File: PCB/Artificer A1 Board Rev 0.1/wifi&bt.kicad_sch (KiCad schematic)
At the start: 13 parts

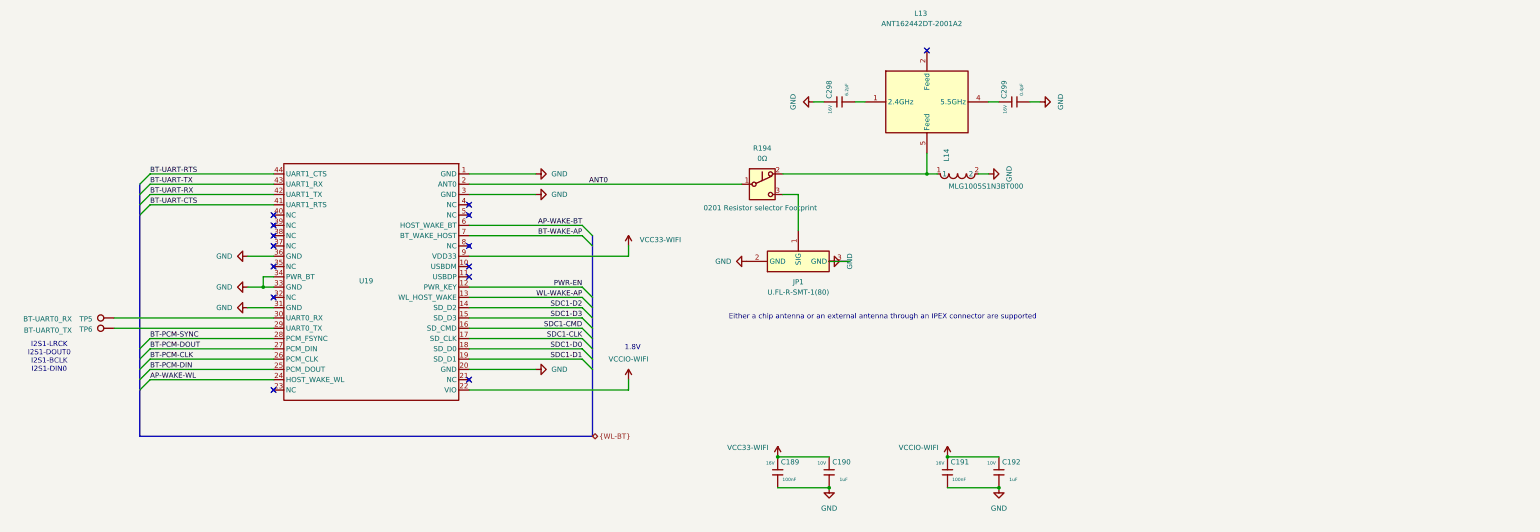
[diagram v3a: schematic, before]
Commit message: optimized copper pour, added LEDs
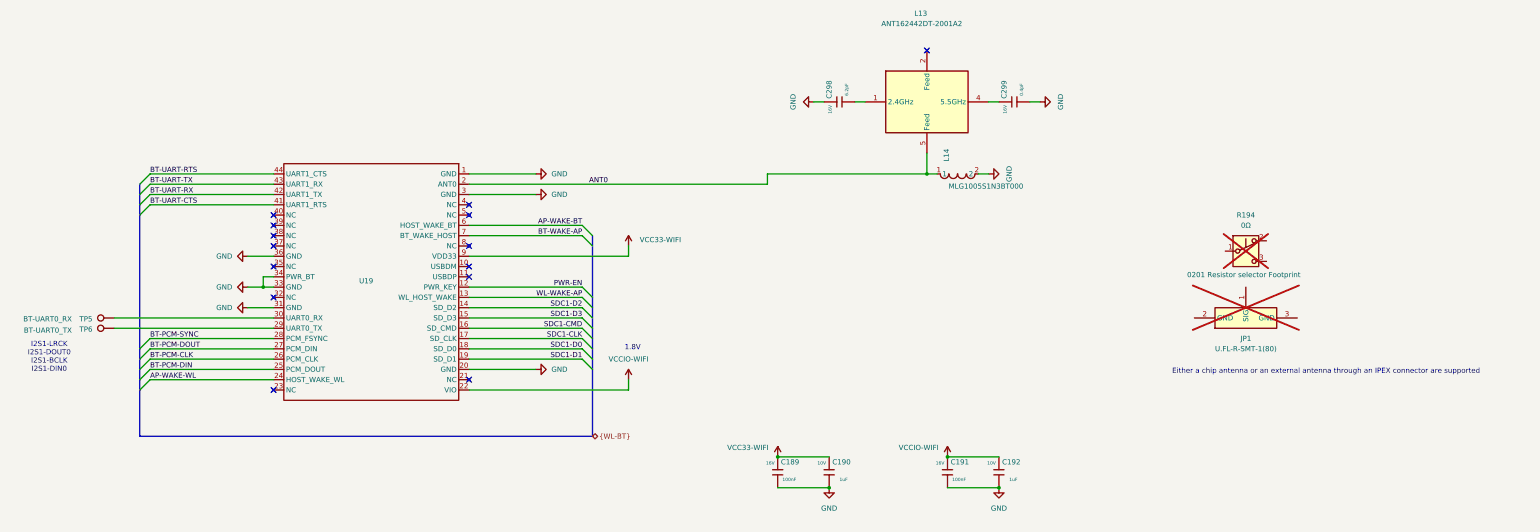
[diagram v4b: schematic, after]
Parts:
- JP1, R194: now not fitted; now left out of the parts list
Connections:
- net ANT0: now also L13.5 (Feed), L14.1; no longer R194.1 (B)
- net GND: no longer JP1.2 (GND), JP1.3 (GND)
- net at R194.3 (C): no longer JP1.1 (SIG)
- now unconnected: R194.2 (A)
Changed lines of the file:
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@@
 	(text "Either a chip antenna or an external antenna through an IPEX connector are supported"
 		(exclude_from_sim no)
-		(at 230.378 107.696 0)
+		(at 339.852 121.158 0)
 		(effects
 			(font
@@
 		)
 	)
-	(bus
+	(wire
 		(pts
-			(xy 158.75 110.49) (xy 158.75 113.03)
+			(xy 201.93 72.39) (xy 201.93 74.93)
 		)
 		(stroke
@@
 		)
 	)
-	(wire
+	(bus
 		(pts
-			(xy 80.01 123.19) (xy 49.53 123.19)
+			(xy 158.75 110.49) (xy 158.75 113.03)
 		)
 		(stroke
@@
 	(wire
 		(pts
-			(xy 205.74 72.39) (xy 241.3 72.39)
+			(xy 80.01 123.19) (xy 49.53 123.19)
 		)
 		(stroke
@@
 		)
 	)
-	(wire
-		(pts
-			(xy 209.55 77.47) (xy 209.55 86.36)
-		)
-		(stroke
-			(width 0)
-			(type default)
-		)
-	)
 	(bus
 		(pts
@@
 	(wire
 		(pts
-			(xy 128.27 74.93) (xy 195.58 74.93)
+			(xy 128.27 74.93) (xy 201.93 74.93)
 		)
 		(stroke
@@
 	(wire
 		(pts
-			(xy 205.74 77.47) (xy 209.55 77.47)
-		)
-		(stroke
-			(width 0)
-			(type default)
-		)
-	)
-	(wire
-		(pts
 			(xy 80.01 100.33) (xy 77.47 100.33)
 		)
@@
 	(wire
 		(pts
-			(xy 215.9 54.61) (xy 213.36 54.61)
+			(xy 201.93 72.39) (xy 241.3 72.39)
 		)
 		(stroke
@@
 	(wire
 		(pts
-			(xy 80.01 72.39) (xy 49.53 72.39)
+			(xy 215.9 54.61) (xy 213.36 54.61)
 		)
 		(stroke
@@
 	(wire
 		(pts
-			(xy 156.21 105.41) (xy 128.27 105.41)
+			(xy 80.01 72.39) (xy 49.53 72.39)
 		)
 		(stroke
@@
 	(wire
 		(pts
-			(xy 80.01 118.11) (xy 49.53 118.11)
+			(xy 156.21 105.41) (xy 128.27 105.41)
 		)
 		(stroke
@@
 	(wire
 		(pts
-			(xy 222.25 93.98) (xy 217.17 93.98)
+			(xy 80.01 118.11) (xy 49.53 118.11)
 		)
 		(stroke
@@
 	)
 	(symbol
-		(lib_id "power:GND")
-		(at 217.17 93.98 90)
-		(mirror x)
-		(unit 1)
-		(body_style 1)
-		(exclude_from_sim no)
-		(in_bom yes)
-		(on_board yes)
-		(in_pos_files yes)
-		(dnp no)
-		(fields_autoplaced yes)
-		(property "Reference" "#PWR0420"
-			(at 223.52 93.98 0)
-			(hide yes)
-			(show_name no)
-			(do_not_autoplace no)
-			(effects
-				(font
-					(size 1.27 1.27)
-				)
-			)
-		)
-		(property "Value" "GND"
-			(at 222.25 93.98 0)
-			(show_name no)
-			(do_not_autoplace no)
-			(effects
-				(font
-					(size 1.27 1.27)
-				)
-			)
-		)
-		(property "Footprint" ""
-			(at 217.17 93.98 0)
-			(hide yes)
-			(show_name no)
-			(do_not_autoplace no)
-			(effects
-				(font
-					(size 1.27 1.27)
-				)
-			)
-		)
-		(property "Datasheet" ""
-			(at 217.17 93.98 0)
-			(hide yes)
-			(show_name no)
-			(do_not_autoplace no)
-			(effects
-				(font
-					(size 1.27 1.27)
-				)
-			)
-		)
-		(property "Description" "Power symbol creates a global label with name \"GND\" , ground"
-			(at 217.17 93.98 0)
-			(hide yes)
-			(show_name no)
-			(do_not_autoplace no)
-			(effects
-				(font
-					(size 1.27 1.27)
-				)
-			)
-		)
-		(pin "1"
-		)
-		(instances
-			(project "Artificer A1 Board Rev 0.1"
-				(path "/7c37bdb5-94b0-4567-b5ec-a879db855389/bb518e39-315f-4fac-931f-ad14a14e5ca9"
-					(reference "#PWR0420")
-					(unit 1)
-				)
-			)
-		)
-	)
-	(symbol
 		(lib_id "easyeda:ANT162442DT-2001A2")
 		(at 241.3 54.61 0)
@@
 	(symbol
 		(lib_id "Switch:SW_Push_SPDT")
-		(at 200.66 74.93 0)
+		(at 320.04 91.44 0)
 		(unit 1)
 		(body_style 1)
-		(exclude_from_sim no)
-		(in_bom yes)
-		(on_board yes)
-		(in_pos_files yes)
-		(dnp no)
+		(exclude_from_sim yes)
+		(in_bom no)
+		(on_board no)
+		(in_pos_files no)
+		(dnp yes)
 		(property "Reference" "R194"
-			(at 200.66 66.04 0)
+			(at 320.04 82.55 0)
 			(show_name no)
 			(do_not_autoplace no)
@@
 		)
 		(property "Value" "0Ω"
-			(at 200.66 68.58 0)
+			(at 320.04 85.09 0)
 			(show_name no)
 			(do_not_autoplace no)
@@
 		)
 		(property "Footprint" "custom footprints:RF_Select_0201_L_Shape"
-			(at 200.66 74.93 0)
+			(at 320.04 91.44 0)
 			(hide yes)
 			(show_name no)
@@
 		)
 		(property "Datasheet" ""
-			(at 200.66 74.93 0)
+			(at 320.04 91.44 0)
 			(hide yes)
 			(show_name no)
@@
 		)
 		(property "Description" "0201 Resistor selector Footprint"
-			(at 200.152 80.772 0)
+			(at 319.532 97.282 0)
 			(show_name no)
 			(do_not_autoplace no)
@@
 	(symbol
 		(lib_id "easyeda:U.FL-R-SMT-1(80)")
-		(at 209.55 91.44 0)
+		(at 320.04 105.41 0)
 		(mirror x)
 		(unit 1)
 		(body_style 1)
-		(exclude_from_sim no)
-		(in_bom yes)
-		(on_board yes)
-		(in_pos_files yes)
-		(dnp no)
+		(exclude_from_sim yes)
+		(in_bom no)
+		(on_board no)
+		(in_pos_files no)
+		(dnp yes)
 		(fields_autoplaced yes)
 		(property "Reference" "JP1"
-			(at 209.55 99.06 0)
+			(at 320.04 113.03 0)
 			(show_name no)
 			(do_not_autoplace no)
@@
 		)
 		(property "Value" "U.FL-R-SMT-1(80)"
-			(at 209.55 101.6 0)
+			(at 320.04 115.57 0)
 			(show_name no)
 			(do_not_autoplace no)
@@
 		)
 		(property "Footprint" "easyeda:RF-SMD_FRF05002-JSS103M"
-			(at 209.55 78.74 0)
+			(at 320.04 92.71 0)
 			(hide yes)
 			(show_name no)
@@
 		)
 		(property "Datasheet" "https://lcsc.com/product-detail/Connectors_HRS_U-FL-R-SMT-1-80_3310472280-IPE-XBoard-end-IPXConnector-SMD_C88374.html"
-			(at 209.55 76.2 0)
+			(at 320.04 90.17 0)
 			(hide yes)
 			(show_name no)
@@
 		)
 		(property "Description" ""
-			(at 209.55 91.44 0)
+			(at 320.04 105.41 0)
 			(hide yes)
 			(show_name no)
@@
 		)
 		(property "LCSC Part" "C88374"
-			(at 209.55 73.66 0)
+			(at 320.04 87.63 0)
 			(hide yes)
 			(show_name no)
@@
 					(unit 1)
 				)
-			)
-		)
-	)
-	(symbol
-		(lib_id "power:GND")
-		(at 196.85 93.98 270)
-		(mirror x)
-		(unit 1)
-		(body_style 1)
-		(exclude_from_sim no)
-		(in_bom yes)
-		(on_board yes)
-		(in_pos_files yes)
-		(dnp no)
-		(fields_autoplaced yes)
-		(property "Reference" "#PWR0417"
-			(at 190.5 93.98 0)
-			(hide yes)
-			(show_name no)
-			(do_not_autoplace no)
-			(effects
-				(font
-					(size 1.27 1.27)
-				)
-			)
-		)
-		(property "Value" "GND"
-			(at 193.04 93.9799 90)
-			(show_name no)
-			(do_not_autoplace no)
-			(effects
-				(font
-					(size 1.27 1.27)
-				)
-				(justify right)
-			)
-		)
-		(property "Footprint" ""
-			(at 196.85 93.98 0)
-			(hide yes)
-			(show_name no)
-			(do_not_autoplace no)
-			(effects
-				(font
-					(size 1.27 1.27)
-				)
-			)
-		)
-		(property "Datasheet" ""
-			(at 196.85 93.98 0)
-			(hide yes)
-			(show_name no)
-			(do_not_autoplace no)
-			(effects
-				(font
-					(size 1.27 1.27)
-				)
-			)
-		)
-		(property "Description" "Power symbol creates a global label with name \"GND\" , ground"
-			(at 196.85 93.98 0)
-			(hide yes)
-			(show_name no)
-			(do_not_autoplace no)
-			(effects
-				(font
-					(size 1.27 1.27)
-				)
-			)
-		)
-		(pin "1"
-		)
-		(instances
-			(project "Artificer A1 Board Rev 0.1"
-				(path "/7c37bdb5-94b0-4567-b5ec-a879db855389/bb518e39-315f-4fac-931f-ad14a14e5ca9"
-					(reference "#PWR0417")
-					(unit 1)
-				)
